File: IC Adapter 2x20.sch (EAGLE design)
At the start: 4 parts, among them IC3 LTC6804IG-1#PBF

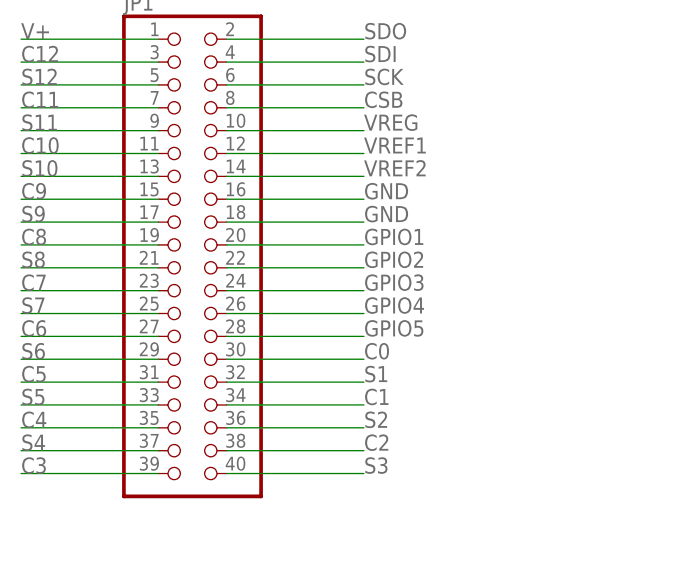
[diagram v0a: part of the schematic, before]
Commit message: IC adapter layouted
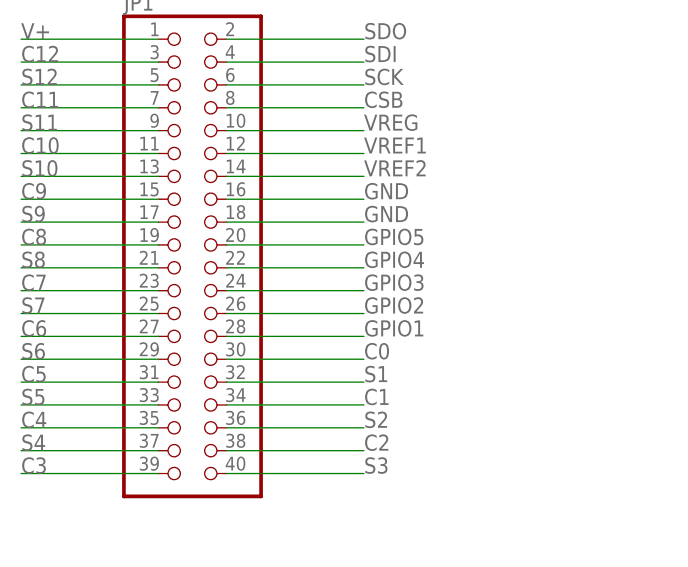
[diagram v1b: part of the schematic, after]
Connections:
- net GPIO1: now also JP1.28; no longer JP1.20
- net GPIO2: now also JP1.26; no longer JP1.22
- net GPIO4: now also JP1.22; no longer JP1.26
- net GPIO5: now also JP1.20; no longer JP1.28
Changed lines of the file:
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@@
 <net name="GPIO1" class="0">
-<segment>
-<pinref part="JP1" gate="A" pin="20"/>
-<wire x1="287.02" y1="309.88" x2="302.26" y2="309.88" width="0.1524" layer="91"/>
-<label x="302.26" y="309.88" size="1.778" layer="95"/>
-</segment>
 <segment>
 <pinref part="IC3" gate="G$1" pin="GPIO1"/>
 <wire x1="297.18" y1="195.58" x2="322.58" y2="195.58" width="0.1524" layer="91"/>
 <label x="304.8" y="195.58" size="1.778" layer="95"/>
+</segment>
+<segment>
+<pinref part="JP1" gate="A" pin="28"/>
+<wire x1="287.02" y1="299.72" x2="302.26" y2="299.72" width="0.1524" layer="91"/>
+<label x="302.26" y="299.72" size="1.778" layer="95"/>
 </segment>
 </net>
@@
 </segment>
 <segment>
-<pinref part="JP1" gate="A" pin="22"/>
-<wire x1="287.02" y1="307.34" x2="302.26" y2="307.34" width="0.1524" layer="91"/>
-<label x="302.26" y="307.34" size="1.778" layer="95"/>
+<pinref part="JP1" gate="A" pin="26"/>
+<wire x1="287.02" y1="302.26" x2="302.26" y2="302.26" width="0.1524" layer="91"/>
+<label x="302.26" y="302.26" size="1.778" layer="95"/>
 </segment>
 </net>
@@
 </segment>
 <segment>
-<pinref part="JP1" gate="A" pin="26"/>
-<wire x1="287.02" y1="302.26" x2="302.26" y2="302.26" width="0.1524" layer="91"/>
-<label x="302.26" y="302.26" size="1.778" layer="95"/>
+<pinref part="JP1" gate="A" pin="22"/>
+<wire x1="287.02" y1="307.34" x2="302.26" y2="307.34" width="0.1524" layer="91"/>
+<label x="302.26" y="307.34" size="1.778" layer="95"/>
 </segment>
 </net>
@@
 </segment>
 <segment>
-<pinref part="JP1" gate="A" pin="28"/>
-<wire x1="287.02" y1="299.72" x2="302.26" y2="299.72" width="0.1524" layer="91"/>
-<label x="302.26" y="299.72" size="1.778" layer="95"/>
+<pinref part="JP1" gate="A" pin="20"/>
+<wire x1="287.02" y1="309.88" x2="302.26" y2="309.88" width="0.1524" layer="91"/>
+<label x="302.26" y="309.88" size="1.778" layer="95"/>
 </segment>
 </net>
